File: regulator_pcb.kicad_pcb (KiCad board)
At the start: 2 copper layers, 28.4 x 9.4 mm, 10 parts, among them J1 Conn_01x02, J2 Conn_01x02, U1 TPS79333-EP

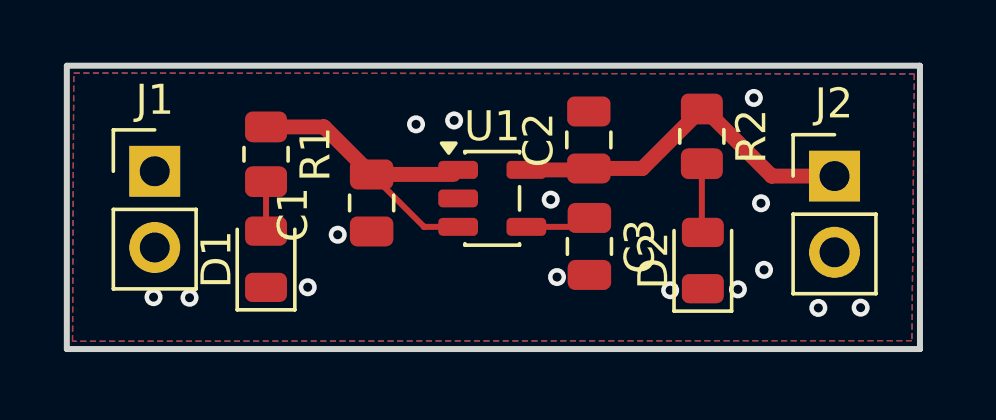
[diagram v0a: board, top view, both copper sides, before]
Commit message: finished copper fill and got everything drc-verified!
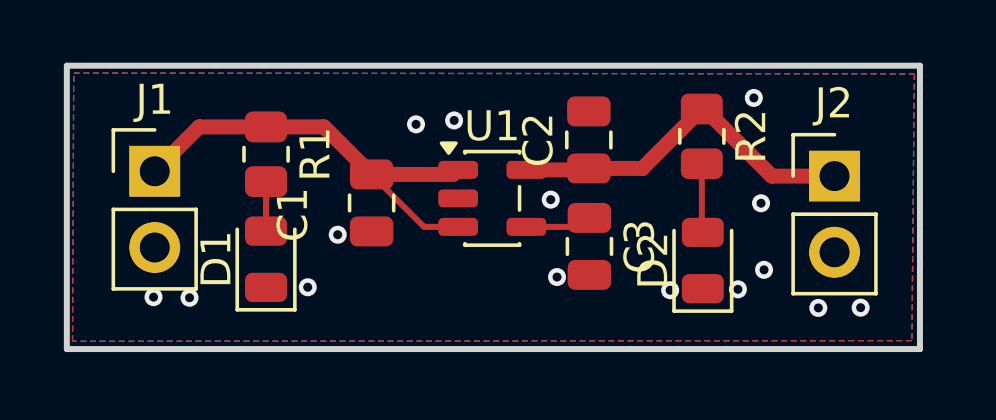
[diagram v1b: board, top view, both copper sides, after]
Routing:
- net Net-(J1-Pin_1): track 10.7 -> 15.1 mm
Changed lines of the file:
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@@
+	)
+	(segment
+		(start 77.87 89.305)
+		(end 75.64 89.305)
+		(width 0.5)
+		(layer "F.Cu")
+		(net "Net-(J1-Pin_1)")
+	)
+	(segment
+		(start 75.64 89.305)
+		(end 74.16 90.785)
+		(width 0.5)
+		(layer "F.Cu")
+		(net "Net-(J1-Pin_1)")
 	)
 	(segment
@@
 		(hatch edge 0.5)
 		(connect_pads yes
-			(clearance 10)
+			(clearance 0.2)
 		)
-		(min_thickness 10)
+		(min_thickness 0.5)
 		(fill yes
-			(thermal_gap 19.68504)
-			(thermal_bridge_width 19.68504)
+			(thermal_gap 1.25)
+			(thermal_bridge_width 1.25)
 			(island_removal_mode 0)
 		)

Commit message: drawing
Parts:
- added G***: LOGO, LOGO, F.Cu at (86.3, 92.1)
